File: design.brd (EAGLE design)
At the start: 150 x 45 mm, 45 parts, among them Q1 16Mhz, Q2 12Mhz, U1 ATMEGA328P-AU, U2 CH340G

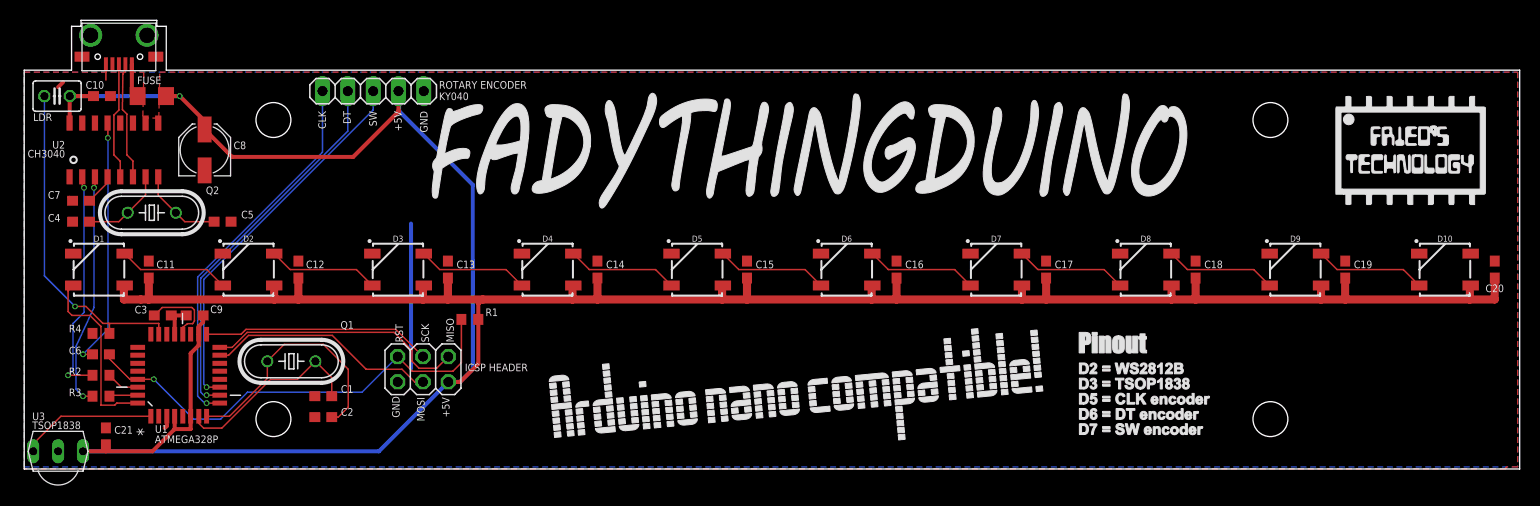
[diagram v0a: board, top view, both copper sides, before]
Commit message: added open hardware logo and fixed an ugly trace
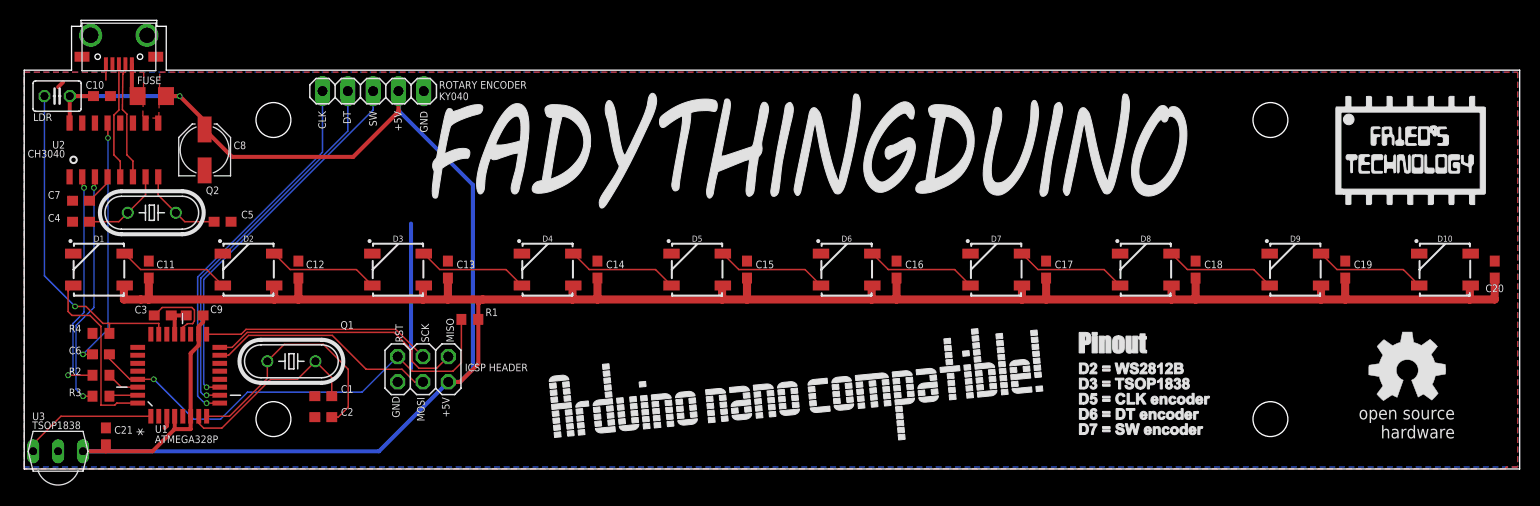
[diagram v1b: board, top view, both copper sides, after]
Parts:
- added U$1: (no value), oshw:OSHW_8MM
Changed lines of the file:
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@@
 <attribute name="VALUE" x="1.014" y="34.352" size="1.27" layer="27" ratio="10"/>
 </element>
+<element name="U$1" library="oshw" package="OSHW_8MM" value="" x="138.7" y="9.9"/>
 </elements>
 <signals>
@@
 <wire x1="7.1" y1="28.7" x2="7.095" y2="28.705" width="0.1524" layer="1"/>
 <wire x1="7.095" y1="28.705" x2="7.095" y2="29.305" width="0.1524" layer="1"/>
-<wire x1="5.9" y1="7.3" x2="5.2024" y2="7.9976" width="0.1524" layer="16"/>
-<wire x1="5.2024" y1="7.9976" x2="5.2024" y2="12.3" width="0.1524" layer="16"/>
-<wire x1="5.2024" y1="12.3" x2="7" y2="16.1976" width="0.1524" layer="16"/>
-<wire x1="7" y1="16.1976" x2="7" y2="28.2" width="0.1524" layer="16"/>
+<wire x1="5.2024" y1="7.9976" x2="5.9" y2="7.3" width="0.1524" layer="16"/>
+<wire x1="7" y1="28.2" x2="7" y2="16.1976" width="0.1524" layer="16"/>
 <contactref element="R3" pad="1"/>
 <wire x1="6.85" y1="7.3" x2="5.9" y2="7.3" width="0.1524" layer="1"/>
+<wire x1="7" y1="16.1976" x2="5.2024" y2="14.4" width="0.1524" layer="16"/>
+<wire x1="5.2024" y1="14.4" x2="5.2024" y2="7.9976" width="0.1524" layer="16"/>
 </signal>
 <signal name="N$6">

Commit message: Minor board updates
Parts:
- moved C5 1.60 mm to (21.5, 24.8)
- moved C4 0.50 mm to (5.20, 24.8)
- moved C7 0.50 mm to (5.20, 26.9)
- moved Q2 0.50 mm to (13.3, 25.7)
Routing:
- net N$9: track 8.55 -> 10.4 mm
- net N$11: track 3.16 -> 4.63 mm
- net N$8: track 8.56 -> 9.35 mm
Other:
- board size 150 x 45 mm -> 150 x 44.8 mm
